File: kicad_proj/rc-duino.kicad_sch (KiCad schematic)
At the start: 53 parts, among them J1 Conn_01x03_Male, J10 Conn_01x04_Male, J11 Conn_01x03_Male, J12 Conn_01x03_Male, J13 Conn_01x02_Male, J14 Conn_01x02_Male, J2 Conn_01x04_Male, J3 Conn_01x02_Male, J4 Conn_01x08_Male, J5 Conn_01x08_Male, J6 Conn_01x08_Male, J7 Conn_01x03_Male, J8 Conn_02x03_Odd_Even, J9 Conn_01x06_Male, U1 rc2014_Ebus-CPU, U2 ATMEGA2560-16AUR, U3 74HCT595D, U4 SN74LVC1G374DCKR, U5 74HCT688, U6 74LVC1G3157, U7 74LVC1G3157, U8 74HCT688, U9 SN74LVC1G08DCKR, Y1 16Mhz Crystal

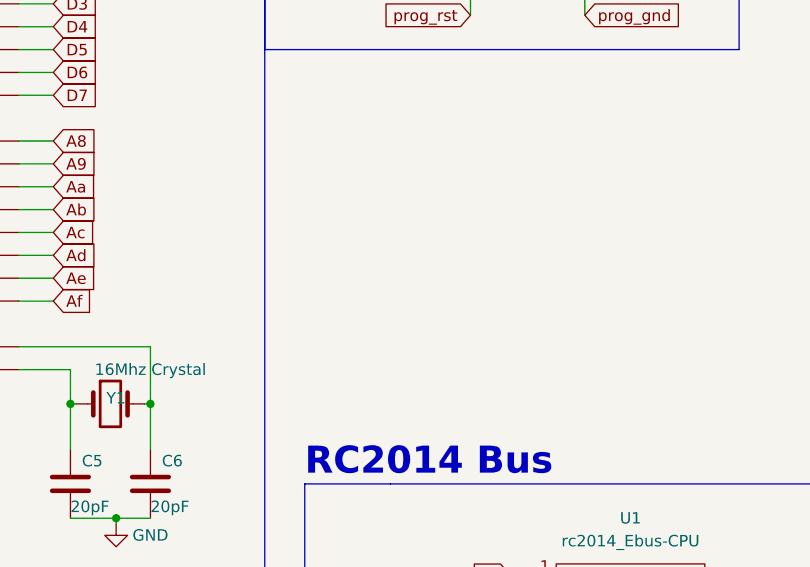
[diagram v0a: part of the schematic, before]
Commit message: revising code into multitasking freeRTOS implementation
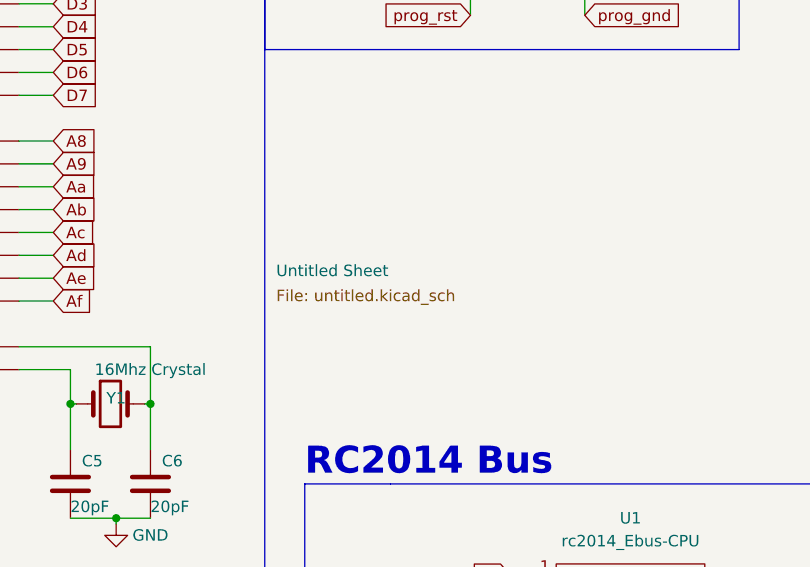
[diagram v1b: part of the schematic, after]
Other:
- added sheet Untitled Sheet (untitled.kicad_sch)
